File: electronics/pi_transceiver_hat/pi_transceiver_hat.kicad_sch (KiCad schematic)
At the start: 7 parts, among them J1 Raspberry_Pi_2_3

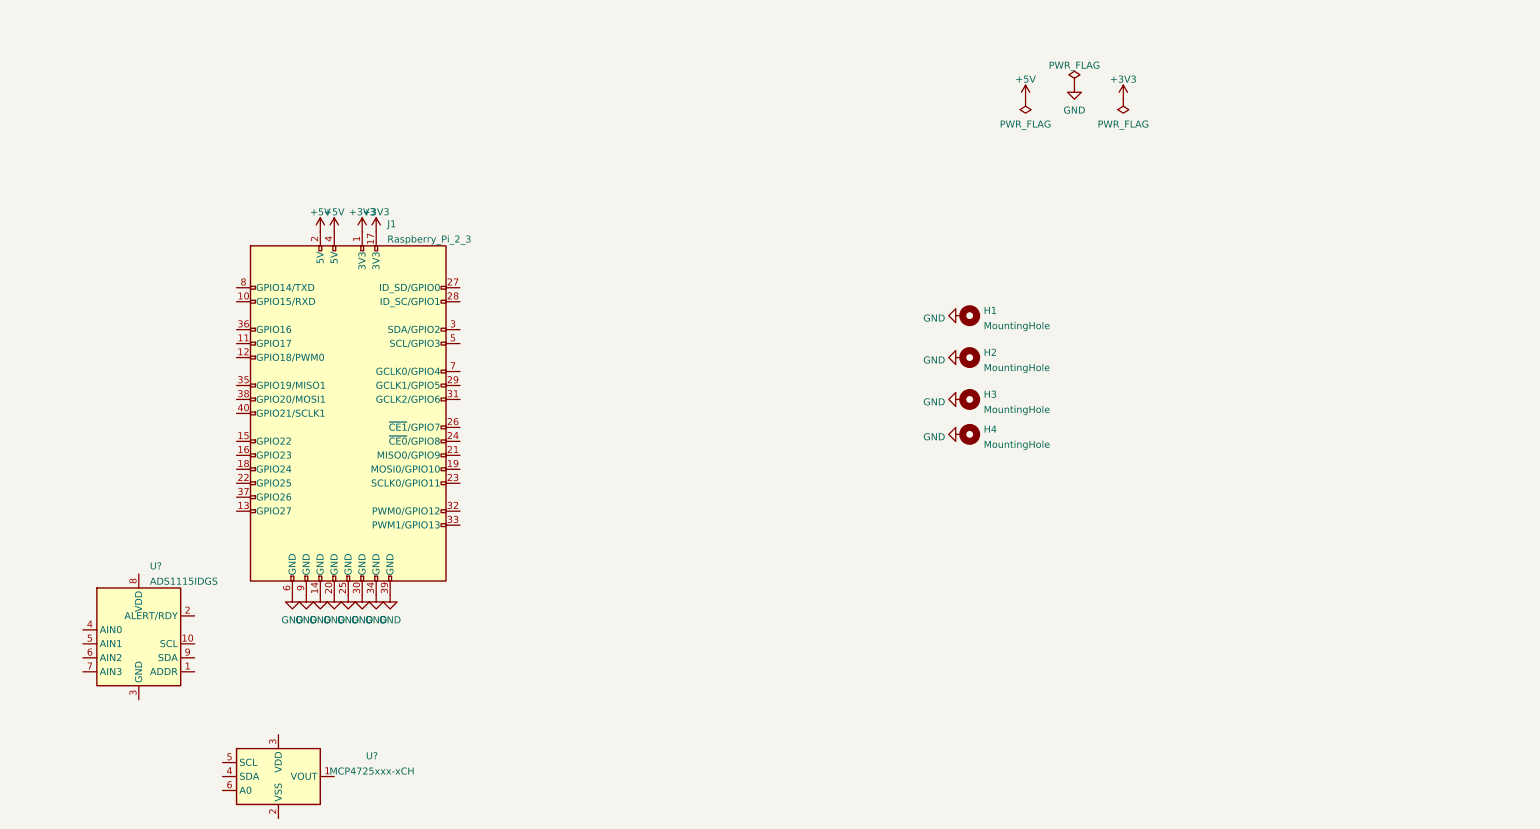
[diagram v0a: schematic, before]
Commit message: Added fan sockets
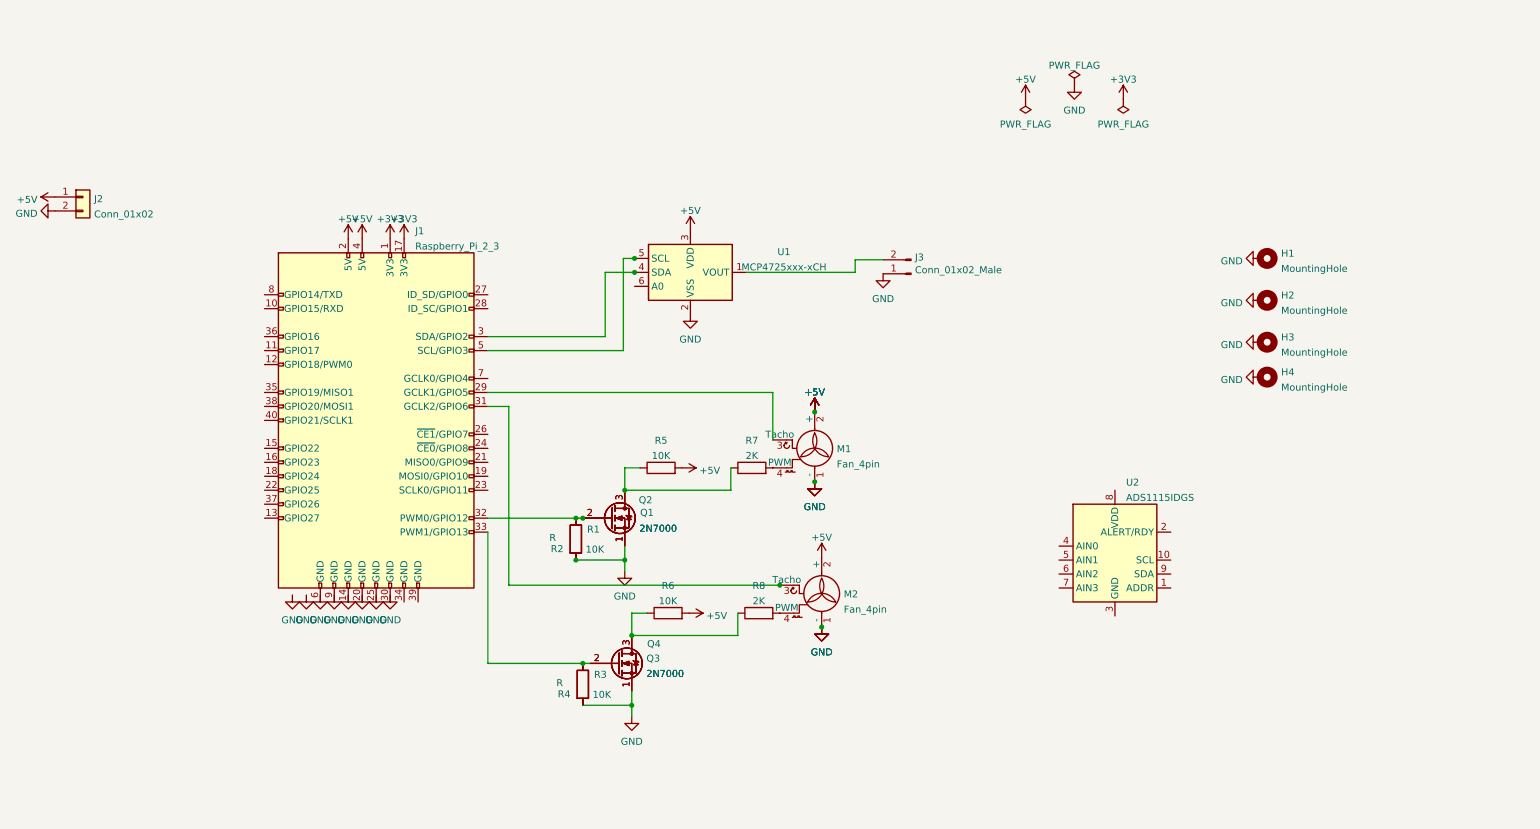
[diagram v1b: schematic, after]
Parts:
- added J2: Conn_01x02, symbol Connector_Generic:Conn_01x02
- added J3: Conn_01x02_Male, Connector_PinHeader_2.54mm:PinHeader_1x02_P2.54mm_Horizontal, symbol Connector:Conn_01x02_Male
- added M1, M2: Fan_4pin, symbol Motor:Fan_4pin
- added Q1, Q2, Q3, Q4: 2N7000, Package_TO_SOT_THT:TO-92_Inline, symbol Transistor_FET:2N7000
- added R1, R3: R, symbol Device:R
- added R2, R4, R5, R6: 10K, symbol Device:R
- added R7, R8: 2K, symbol Device:R
- gave numbers to parts that had none: 2
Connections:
- net +5V: now also U1.3 (VDD), J2.1 (Pin_1), M1.2 (+), M2.2 (+), R5.2, R6.2
- net GND: now also U1.2 (VSS), J2.2 (Pin_2), J3.1 (Pin_1), M1.1 (-), M2.1 (-), Q1.1 (S), Q2.1 (S), Q3.1 (S), Q4.1 (S), R1.2, R2.2, R3.2, R4.2; no longer J1.14 (GND), J1.20 (GND), J1.25 (GND), J1.30 (GND), J1.34 (GND), J1.39 (GND), J1.6 (GND), J1.9 (GND)
- net at U1.1 (VOUT): now also J3.2 (Pin_2)
- net at U1.4 (SDA): now also J1.3 (SDA/GPIO2)
- net at U1.5 (SCL): now also J1.5 (SCL/GPIO3)
- net at J1.29 (GCLK1/GPIO5): now also M1.3 (Tacho)
- net at J1.31 (GCLK2/GPIO6): now also M2.3 (Tacho)
- net at J1.32 (PWM0/GPIO12): now also Q1.2 (G), Q2.2 (G), R1.1, R2.1
- net at J1.33 (PWM1/GPIO13): now also Q3.2 (G), Q4.2 (G), R3.1, R4.1
- new net: Q3.3 (D), Q4.3 (D), R6.1, R8.1
- new net: M1.4 (PWM), R7.2
- new net: M2.4 (PWM), R8.2
- new net: Q1.3 (D), Q2.3 (D), R5.1, R7.1
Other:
- moved on the sheet: H1, H2, H3, H4, J1, U1, U2

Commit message: More PCB hat design
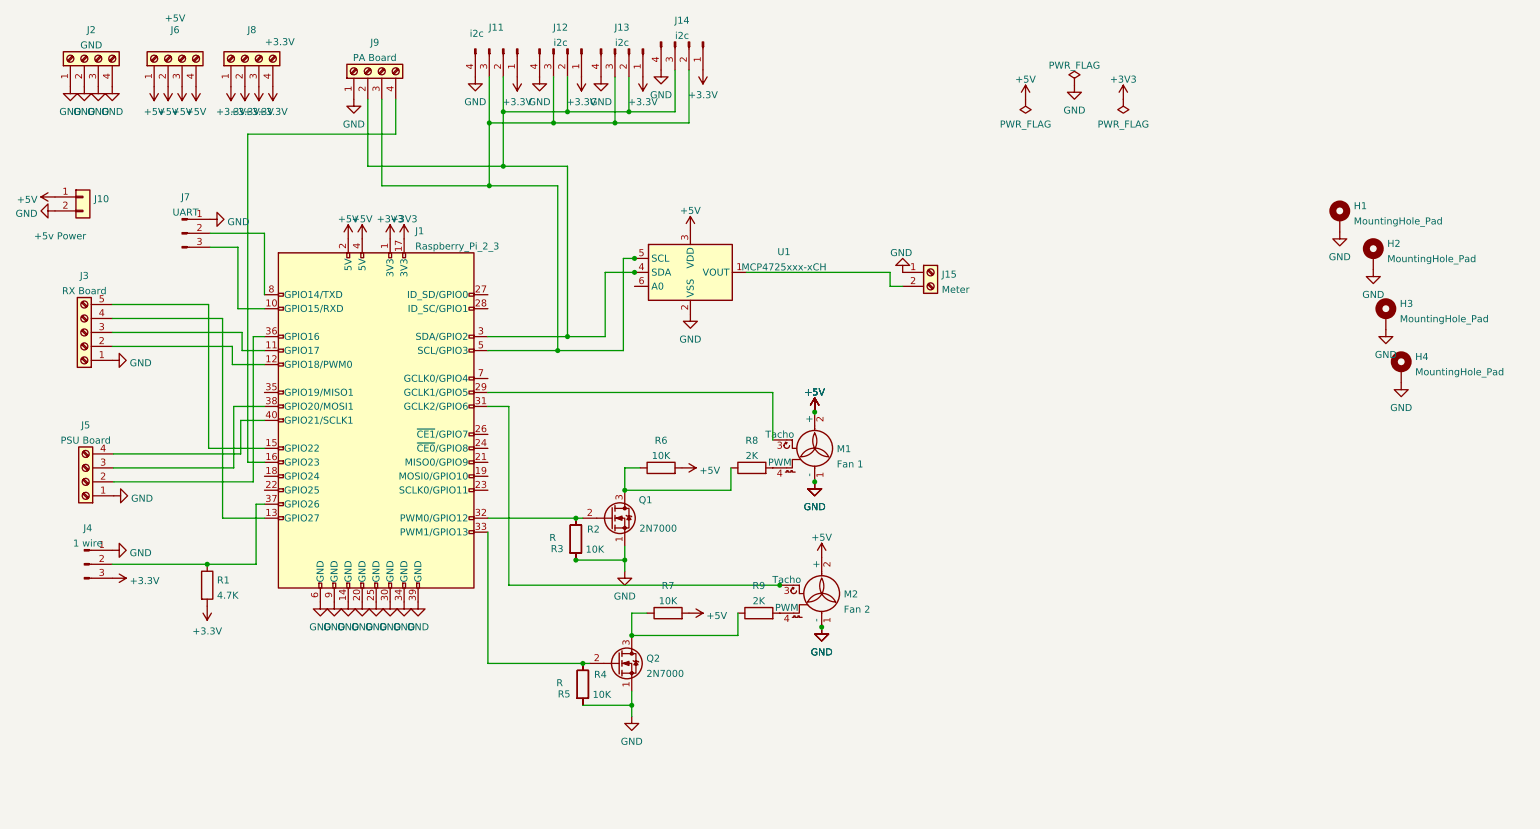
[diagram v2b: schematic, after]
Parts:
- removed H1, H2, H3, H4: MountingHole, MountingHole:MountingHole_2.7mm_M2.5_ISO14580_Pad, symbol Mechanical:MountingHole
- removed J3: Conn_01x02_Male, Connector_PinHeader_2.54mm:PinHeader_1x02_P2.54mm_Horizontal, symbol Connector:Conn_01x02_Male
- removed Q1, Q4: 2N7000, Package_TO_SOT_THT:TO-92_Inline, symbol Transistor_FET:2N7000
- removed U2: ADS1115IDGS, Package_SO:TSSOP-10_3x3mm_P0.5mm, symbol Analog_ADC:ADS1115IDGS
- added H1, H2, H3, H4: MountingHole_Pad, MountingHole:MountingHole_2.7mm_M2.5, symbol Mechanical:MountingHole_Pad
- added J11, J12, J13, J14: i2c, Connector_JST:JST_GH_BM04B-GHS-TBT_1x04-1MP_P1.25mm_Vertical, symbol Connector:Conn_01x04_Male
- added J15: Meter, TerminalBlock_TE-Connectivity:TerminalBlock_TE_282834-2_1x02_P2.54mm_Horizontal, symbol Connector:Screw_Terminal_01x02
- added J2: GND, TerminalBlock_TE-Connectivity:TerminalBlock_TE_282834-4_1x04_P2.54mm_Horizontal, symbol Connector:Screw_Terminal_01x04
- added J3: RX Board, TerminalBlock_TE-Connectivity:TerminalBlock_TE_282834-5_1x05_P2.54mm_Horizontal, symbol Connector:Screw_Terminal_01x05
- added J4: 1 wire, TerminalBlock_TE-Connectivity:TerminalBlock_TE_282834-3_1x03_P2.54mm_Horizontal, symbol Connector:Conn_01x03_Male
- added J5: PSU Board, TerminalBlock_TE-Connectivity:TerminalBlock_TE_282834-4_1x04_P2.54mm_Horizontal, symbol Connector:Screw_Terminal_01x04
- added J6: +5V, TerminalBlock_TE-Connectivity:TerminalBlock_TE_282834-4_1x04_P2.54mm_Horizontal, symbol Connector:Screw_Terminal_01x04
- added J7: UART, Connector_JST:JST_JWPF_B03B-JWPF-SK-R_1x03_P2.00mm_Vertical, symbol Connector:Conn_01x03_Male
- added J8: +3.3V, TerminalBlock_TE-Connectivity:TerminalBlock_TE_282834-4_1x04_P2.54mm_Horizontal, symbol Connector:Screw_Terminal_01x04
- added J9: PA Board, TerminalBlock_TE-Connectivity:TerminalBlock_TE_282834-4_1x04_P2.54mm_Horizontal, symbol Connector:Screw_Terminal_01x04
- added R1: 4.7K, Resistor_SMD:R_0805_2012Metric_Pad1.20x1.40mm_HandSolder, symbol Device:R
- J10: renamed from J2; value Conn_01x02 -> +5v Power; footprint (none) -> TerminalBlock_TE-Connectivity:TerminalBlock_TE_282834-2_1x02_P2.54mm_Horizontal
- M1: value Fan_4pin -> Fan 1; footprint (none) -> Connector_Molex:Molex_KK-254_AE-6410-04A_1x04_P2.54mm_Vertical
- M2: value Fan_4pin -> Fan 2; footprint (none) -> Connector_Molex:Molex_KK-254_AE-6410-04A_1x04_P2.54mm_Vertical
- Q1: renamed from Q2; footprint Package_TO_SOT_THT:TO-92_Inline -> Package_TO_SOT_SMD:SOT-23
- Q2: renamed from Q3; footprint Package_TO_SOT_THT:TO-92_Inline -> Package_TO_SOT_SMD:SOT-23
- R2: renamed from R1; footprint (none) -> Resistor_SMD:R_0805_2012Metric_Pad1.20x1.40mm_HandSolder
- R3: renamed from R2; footprint (none) -> Resistor_SMD:R_0805_2012Metric_Pad1.20x1.40mm_HandSolder
- R4: renamed from R3; footprint (none) -> Resistor_SMD:R_0805_2012Metric_Pad1.20x1.40mm_HandSolder
- R5: renamed from R4; footprint (none) -> Resistor_SMD:R_0805_2012Metric_Pad1.20x1.40mm_HandSolder
- R6: renamed from R5; footprint (none) -> Resistor_SMD:R_0805_2012Metric_Pad1.20x1.40mm_HandSolder
- R7: renamed from R6; footprint (none) -> Resistor_SMD:R_0805_2012Metric_Pad1.20x1.40mm_HandSolder
- R8: renamed from R7; footprint (none) -> Resistor_SMD:R_0805_2012Metric_Pad1.20x1.40mm_HandSolder
- R9: renamed from R8; footprint (none) -> Resistor_SMD:R_0805_2012Metric_Pad1.20x1.40mm_HandSolder
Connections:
- net +3V3: now also J11.1 (Pin_1), J12.1 (Pin_1), J13.1 (Pin_1), J14.1 (Pin_1), J4.3 (Pin_3), J8.1 (Pin_1), J8.2 (Pin_2), J8.3 (Pin_3), J8.4 (Pin_4), R1.2
- net +5V: now also J6.1 (Pin_1), J6.2 (Pin_2), J6.3 (Pin_3), J6.4 (Pin_4)
- net GND: now also J1.14 (GND), J1.20 (GND), J1.25 (GND), J1.30 (GND), J1.34 (GND), J1.39 (GND), J1.6 (GND), J1.9 (GND), H1.1, H2.1, H3.1, H4.1, J11.4 (Pin_4), J12.4 (Pin_4), J13.4 (Pin_4), J14.4 (Pin_4), J15.1 (Pin_1), J2.1 (Pin_1), J2.2 (Pin_2), J2.3 (Pin_3), J2.4 (Pin_4), J3.1 (Pin_1), J4.1 (Pin_1), J5.1 (Pin_1), J7.1 (Pin_1), J9.1 (Pin_1)
- net at U1.1 (VOUT): now also J15.2 (Pin_2)
- net at J1.3 (SDA/GPIO2), U1.4 (SDA): now also J11.2 (Pin_2), J12.2 (Pin_2), J13.2 (Pin_2), J14.3 (Pin_3), J9.2 (Pin_2)
- net at J1.5 (SCL/GPIO3), U1.5 (SCL): now also J11.3 (Pin_3), J12.3 (Pin_3), J13.3 (Pin_3), J14.2 (Pin_2), J9.3 (Pin_3)
- net at J1.10 (GPIO15/RXD): now also J7.3 (Pin_3)
- net at J1.11 (GPIO17): now also J3.3 (Pin_3)
- net at J1.12 (GPIO18/PWM0): now also J3.2 (Pin_2)
- net at J1.13 (GPIO27): now also J3.4 (Pin_4)
- net at J1.15 (GPIO22): now also J3.5 (Pin_5)
- net at J1.16 (GPIO23): now also J9.4 (Pin_4)
- net at J1.36 (GPIO16): now also J5.2 (Pin_2)
- net at J1.37 (GPIO26): now also J4.2 (Pin_2), R1.1
- net at J1.38 (GPIO20/MOSI1): now also J5.3 (Pin_3)
- net at J1.40 (GPIO21/SCLK1): now also J5.4 (Pin_4)
- net at J1.8 (GPIO14/TXD): now also J7.2 (Pin_2)

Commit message: More hat board design.
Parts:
- removed R2, R4: R, Resistor_SMD:R_0805_2012Metric_Pad1.20x1.40mm_HandSolder, symbol Device:R
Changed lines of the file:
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@@
   (junction (at 126.492 130.556) (diameter 0) (color 0 0 0 0)
-  )
-  (junction (at 125.222 111.76) (diameter 0) (color 0 0 0 0)
   )
   (junction (at 109.474 32.258) (diameter 0) (color 0 0 0 0)
@@
     )
     (pin "1")
-  )
-  (symbol (lib_id "Device:R") (at 125.222 107.95 0) (unit 1)
-    (in_bom yes) (on_board yes)
-    (property "Reference" "R2" (id 0) (at 127.254 106.172 0)
-      (effects (font (size 1.27 1.27)) (justify left))
-    )
-    (property "Value" "R" (id 1) (at 120.396 107.696 0)
-      (effects (font (size 1.27 1.27)) (justify left))
-    )
-    (property "Footprint" "Resistor_SMD:R_0805_2012Metric_Pad1.20x1.40mm_HandSolder" (id 2) (at 123.444 107.95 90)
-      (effects (font (size 1.27 1.27)) hide)
-    )
-    (property "Datasheet" "~" (id 3) (at 125.222 107.95 0)
-      (effects (font (size 1.27 1.27)) hide)
-    )
-    (pin "1")
-    (pin "2")
   )
   (symbol (lib_id "power:PWR_FLAG") (at 215.9 25.4 0) (unit 1)
@@
     (pin "4")
   )
-  (symbol (lib_id "Device:R") (at 126.492 134.366 0) (unit 1)
-    (in_bom yes) (on_board yes)
-    (property "Reference" "R4" (id 0) (at 128.524 132.588 0)
-      (effects (font (size 1.27 1.27)) (justify left))
-    )
-    (property "Value" "R" (id 1) (at 121.666 134.112 0)
-      (effects (font (size 1.27 1.27)) (justify left))
-    )
-    (property "Footprint" "Resistor_SMD:R_0805_2012Metric_Pad1.20x1.40mm_HandSolder" (id 2) (at 124.714 134.366 90)
-      (effects (font (size 1.27 1.27)) hide)
-    )
-    (property "Datasheet" "~" (id 3) (at 126.492 134.366 0)
-      (effects (font (size 1.27 1.27)) hide)
-    )
-    (pin "1")
-    (pin "2")
-  )
   (symbol (lib_id "power:GND") (at 84.836 27.94 0) (unit 1)
     (in_bom yes) (on_board yes) (fields_autoplaced)
@@
       (reference "R1") (unit 1) (value "4.7K") (footprint "Resistor_SMD:R_0805_2012Metric_Pad1.20x1.40mm_HandSolder")
     )
-    (path "/92cc5a73-ad10-4c74-9cf9-f50cd9f30783"
-      (reference "R2") (unit 1) (value "R") (footprint "Resistor_SMD:R_0805_2012Metric_Pad1.20x1.40mm_HandSolder")
-    )
     (path "/e0fcac20-9b7d-4484-b069-ebe3adefc896"
       (reference "R3") (unit 1) (value "10K") (footprint "Resistor_SMD:R_0805_2012Metric_Pad1.20x1.40mm_HandSolder")
     )
-    (path "/a48f26a0-7709-4f63-bae8-7a05c4e18a8c"
-      (reference "R4") (unit 1) (value "R") (footprint "Resistor_SMD:R_0805_2012Metric_Pad1.20x1.40mm_HandSolder")
-    )
     (path "/a9ee0268-3822-4209-bb25-7b9b50195d68"

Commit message: PCB updates for hat.
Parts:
- added C1: 10uF, Capacitor_SMD:CP_Elec_10x12.6, symbol Device:C_Polarized
- added C2: 100nF, Capacitor_SMD:C_0805_2012Metric_Pad1.18x1.45mm_HandSolder, symbol Device:C
- added C3, C4, C5: C, Capacitor_SMD:C_0805_2012Metric_Pad1.18x1.45mm_HandSolder, symbol Device:C
- added R10, R2, R4: 4.7K, Resistor_SMD:R_0805_2012Metric_Pad1.20x1.40mm_HandSolder, symbol Device:R
- added R11: 0R, Resistor_SMD:R_0805_2012Metric_Pad1.20x1.40mm_HandSolder, symbol Device:R
- J11, J12, J13, J14: footprint Connector_JST:JST_GH_BM04B-GHS-TBT_1x04-1MP_P1.25mm_Vertical -> Connector_JST:JST_XH_B4B-XH-A_1x04_P2.50mm_Vertical
- J7: footprint Connector_JST:JST_JWPF_B03B-JWPF-SK-R_1x03_P2.00mm_Vertical -> Connector_JST:JST_XH_B3B-XH-A_1x03_P2.50mm_Vertical
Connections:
- net +3V3: now also R2.2, R4.2
- net +5V: now also C1.1, C5.1, R10.1
- net GND: now also C1.2, C2.2, C3.1, C4.1, C5.2, R11.2
- net at J1.37 (GPIO26), J4.2 (Pin_2), R1.1: now also C2.1
- net at J1.3 (SDA/GPIO2), J11.2 (Pin_2), J12.2 (Pin_2)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: now also C4.2, R4.1
- net at J1.5 (SCL/GPIO3), J11.3 (Pin_3), J12.3 (Pin_3)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: now also C3.2, R2.1
- net at U1.6 (A0): now also R10.2, R11.1
- no-connect marks 0 -> 11
